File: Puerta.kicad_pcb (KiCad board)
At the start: 4 copper layers, 72.5 x 76.4 mm, 73 parts, among them J100 VCC INPUT, J101 SWITCH ON/OFF, J102 FAN VOLTAGE, J200 Serial Wire Debug, J201 CAN_ID_CONFIG, J202 CAN_INPUT, J204 JUMPER_CAN, J300 DOOR_OUTPUT, J301 Panic_Button, J302 Door_Sensor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

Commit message: added logo
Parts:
- added G***: LOGO, LOGO, F.Cu at (113.9, 76.5)
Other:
- board text added: "BOTON PANICO"
- board text added: "SENSOR PUERTA"
- board text added: "VCC"
- board text removed: "INPUT"
- board text removed: "OUTPUT"
- board text removed: "PANIC BUTTON"
- board text removed: "SENSOR DOOR"

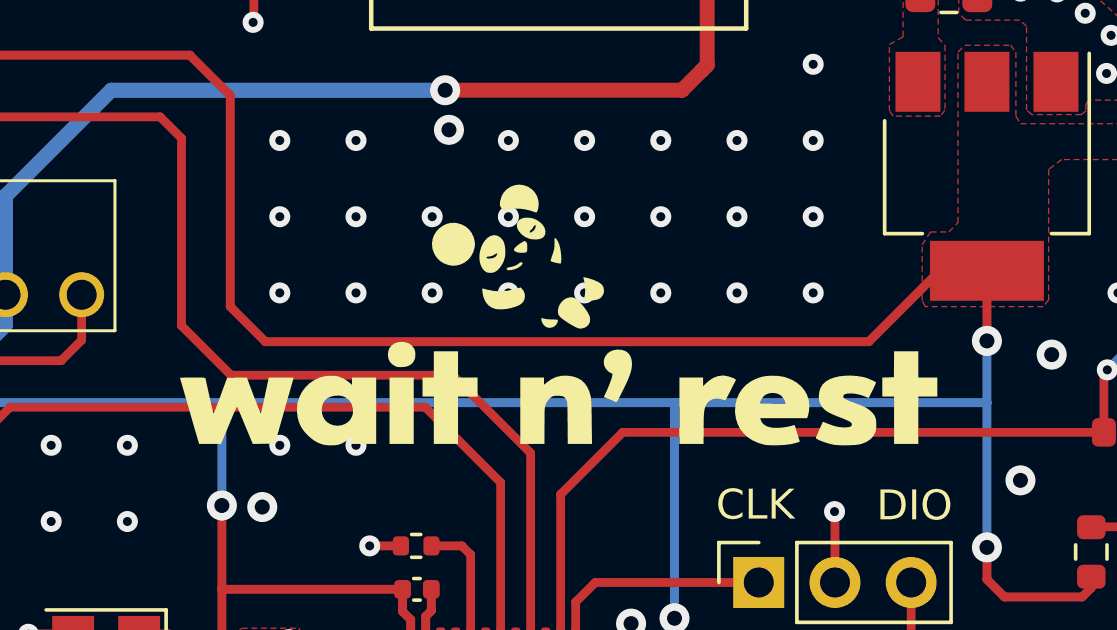
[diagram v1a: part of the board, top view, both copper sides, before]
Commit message: change board stackup and added logo
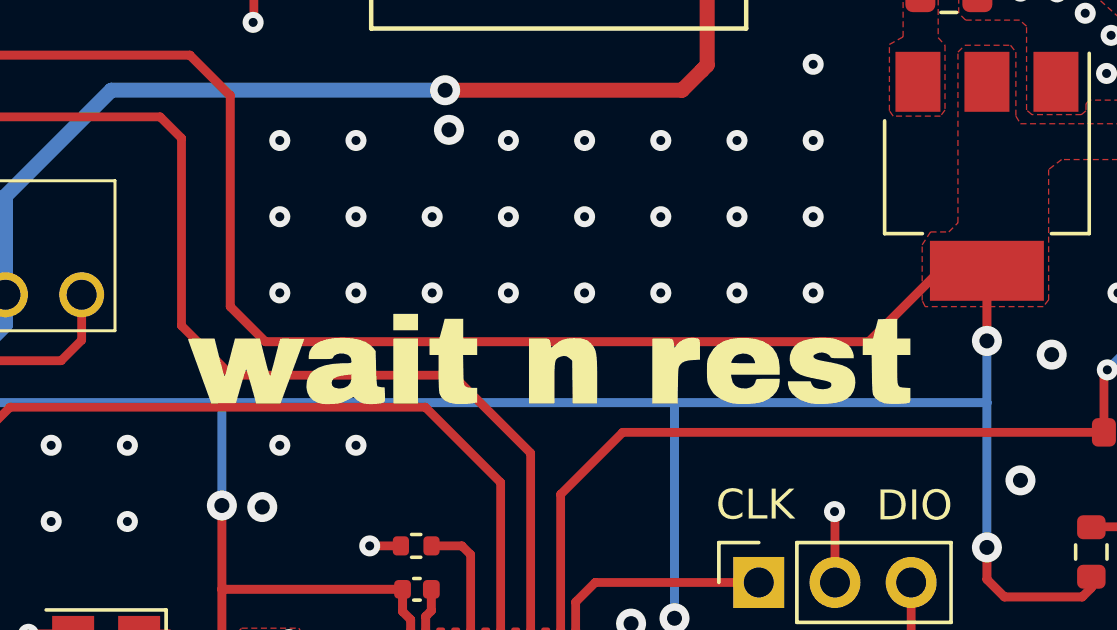
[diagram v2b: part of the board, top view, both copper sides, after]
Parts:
- moved G*** 0.94 mm to (113.1, 75.9)

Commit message: version validada
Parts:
- J101: footprint Connector_PinHeader_2.54mm:PinHeader_1x02_P2.54mm_Vertical -> B2B-XH-A:JST_B2B-XH-A_LF__SN_
- L100: footprint Jose_:SMD_12.3X12.3mm -> Inductor_SMD_Jose:L_12.3x12.3
- moved TP101 4.15 mm to (75.8, 52.9)
- moved TP100 2.86 mm to (71.3, 52.9)
- moved J101 2.54 mm to (72.7, 45.6)
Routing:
- net /POWER/V_INPUT: track 25.6 -> 29.2 mm
- net /POWER/switch: track 9.61 -> 12.5 mm
- net GND: track 79.8 -> 80.5 mm, vias 242 -> 237
